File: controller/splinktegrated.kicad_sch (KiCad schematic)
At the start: 41 parts, among them J1 USB_C_Receptacle_USB2.0, J11 Conn_01x07_Socket, J2 Conn_01x04_Socket, J5 Conn_01x02, J7 Cirque, SW2 NA_SW_SPST, U1 RP2040, U3 XC6210B332MR-G, U4 USBLC6-2P6, U5 W25Q128JVS, Y1 Crystal_GND24

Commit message: work
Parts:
- J2: footprint Connector_PinSocket_2.54mm:PinSocket_1x04_P2.54mm_Vertical -> Library:PinSocket_1x04_P2.54mm_Vertical
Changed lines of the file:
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@@
 			)
 		)
-		(property "Footprint" "Connector_PinSocket_2.54mm:PinSocket_1x04_P2.54mm_Vertical"
+		(property "Footprint" "Library:PinSocket_1x04_P2.54mm_Vertical"
 			(at 396.24 38.1 0)
 			(effects

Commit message: Update splinktegrated.kicad_sch
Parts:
- removed SW2: NA_SW_SPST, Library:PushSwitch, symbol Switch:SW_SPST
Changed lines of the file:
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@@
 		)
 	)
-	(label "~{RESET}"
-		(at 44.45 205.105 180)
-		(fields_autoplaced yes)
-		(effects
-			(font
-				(size 1.27 1.27)
-			)
-			(justify right bottom)
-		)
-	)
 	(label "QSPI_~{CS}"
 		(at 111.76 59.69 0)
@@
 	)
 	(symbol
-		(lib_id "Switch:SW_SPST")
-		(at 49.53 205.105 0)
-		(unit 1)
-		(exclude_from_sim no)
-		(in_bom no)
-		(on_board yes)
-		(dnp no)
-		(property "Reference" "SW2"
-			(at 49.53 198.755 0)
-			(effects
-				(font
-					(size 1.27 1.27)
-				)
-			)
-		)
-		(property "Value" "NA_SW_SPST"
-			(at 49.53 201.295 0)
-			(effects
-				(font
-					(size 1.27 1.27)
-				)
-			)
-		)
-		(property "Footprint" "Library:PushSwitch"
-			(at 49.53 205.105 0)
-			(effects
-				(font
-					(size 1.27 1.27)
-				)
-				(hide yes)
-			)
-		)
-		(property "Datasheet" "~"
-			(at 49.53 205.105 0)
-			(effects
-				(font
-					(size 1.27 1.27)
-				)
-				(hide yes)
-			)
-		)
-		(property "Description" ""
-			(at 49.53 205.105 0)
-			(effects
-				(font
-					(size 1.27 1.27)
-				)
-				(hide yes)
-			)
-		)
-		(pin "1"
-		)
-		(pin "2"
-		)
-		(instances
-			(project "splinktegrated"
-				(path "/7353e96a-343a-4876-b497-b1d205a14d97"
-					(reference "SW2")
-					(unit 1)
-				)
-			)
-		)
-	)
-	(symbol
 		(lib_id "power:+1V1")
 		(at 91.44 173.99 0)
@@
 					(unit 1)
 				)
-			)
-		)
-	)
-	(symbol
-		(lib_id "power:GND")
-		(at 54.61 205.105 90)
-		(unit 1)
-		(exclude_from_sim no)
-		(in_bom yes)
-		(on_board yes)
-		(dnp no)
-		(property "Reference" "#PWR05"
-			(at 60.96 205.105 0)
-			(effects
-				(font
-					(size 1.27 1.27)
-				)
-				(hide yes)
-			)
-		)
-		(property "Value" "GND"
-			(at 61.5949 205.261 90)
-			(effects
-				(font
-					(size 1.27 1.27)
-				)
-				(justify left)
-			)
-		)
-		(property "Footprint" ""
-			(at 54.61 205.105 0)
-			(effects
-				(font
-					(size 1.27 1.27)
-				)
-				(hide yes)
-			)
-		)
-		(property "Datasheet" ""
-			(at 54.61 205.105 0)
-			(effects
-				(font
-					(size 1.27 1.27)
-				)
-				(hide yes)
-			)
-		)
-		(property "Description" ""
-			(at 54.61 205.105 0)
-			(effects
-				(font
-					(size 1.27 1.27)
-				)
-				(hide yes)
-			)
-		)
-		(pin "1"
-		)
-		(instances
-			(project "splinktegrated"
-				(path "/7353e96a-343a-4876-b497-b1d205a14d97"
-					(reference "#PWR05")
-					(unit 1)
-				)

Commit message: work
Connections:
- net VBUS renamed Vbus_daughter
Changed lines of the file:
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@@
 	)
 	(junction
-		(at 29.845 29.845)
-		(diameter 0)
-		(color 0 0 0 0)
-	)
-	(junction
 		(at 143.51 38.1)
 		(diameter 0)
@@
 	(wire
 		(pts
-			(xy 27.305 29.845) (xy 29.845 29.845)
+			(xy 27.305 29.845) (xy 32.385 29.845)
 		)
 		(stroke
@@
 		)
 	)
-	(wire
-		(pts
-			(xy 29.845 26.035) (xy 29.845 29.845)
-		)
-		(stroke
-			(width 0)
-			(type default)
-		)
-	)
 	(polyline
 		(pts
@@
 	(wire
 		(pts
-			(xy 29.845 29.845) (xy 32.385 29.845)
-		)
-		(stroke
-			(width 0)
-			(type default)
-		)
-	)
-	(wire
-		(pts
 			(xy 101.6 173.99) (xy 101.6 175.26)
 		)
@@
 					(unit 1)
 				)
-			)
-		)
-	)
-	(symbol
-		(lib_id "power:VBUS")
-		(at 29.845 26.035 0)
-		(unit 1)
-		(exclude_from_sim no)
-		(in_bom yes)
-		(on_board yes)
-		(dnp no)
-		(property "Reference" "#PWR0104"
-			(at 29.845 29.845 0)
-			(effects
-				(font
-					(size 1.27 1.27)
-				)
-				(hide yes)
-			)
-		)
-		(property "Value" "VBUS"
-			(at 29.845 22.225 0)
-			(effects
-				(font
-					(size 1.27 1.27)
-				)
-			)
-		)
-		(property "Footprint" ""
-			(at 29.845 26.035 0)
-			(effects
-				(font
-					(size 1.27 1.27)
-				)
-				(hide yes)
-			)
-		)
-		(property "Datasheet" ""
-			(at 29.845 26.035 0)
-			(effects
-				(font
-					(size 1.27 1.27)
-				)
-				(hide yes)
-			)
-		)
-		(property "Description" ""
-			(at 29.845 26.035 0)
-			(effects
-				(font
-					(size 1.27 1.27)
-				)
-				(hide yes)
-			)
-		)
-		(pin "1"
-		)
-		(instances
-			(project "splinktegrated"
-				(path "/7353e96a-343a-4876-b497-b1d205a14d97"
-					(reference "#PWR0104")
-					(unit 1)
-				)

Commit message: details
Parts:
- removed H1, H2: NA_M4, drawings:MountingHole_3mm_Pad_Via, symbol Mechanical:MountingHole_Pad
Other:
- note removed: "Plate screws"

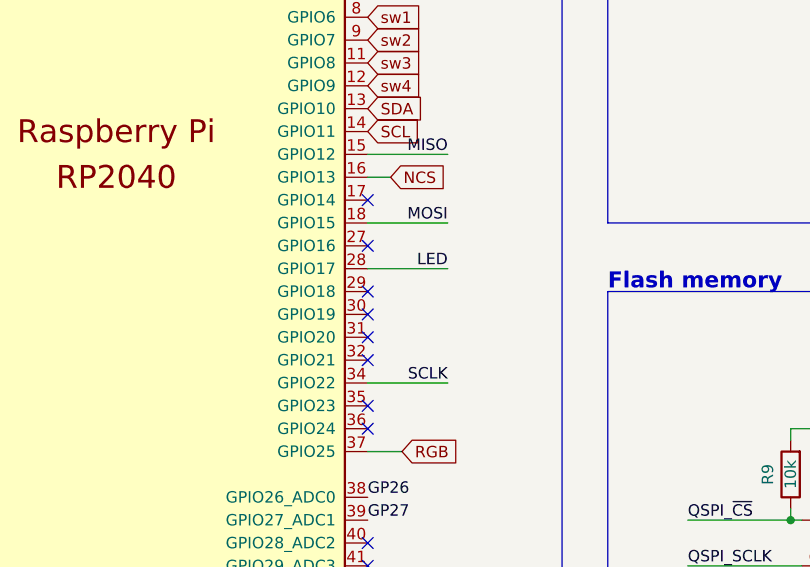
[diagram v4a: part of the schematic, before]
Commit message: change SCK pin
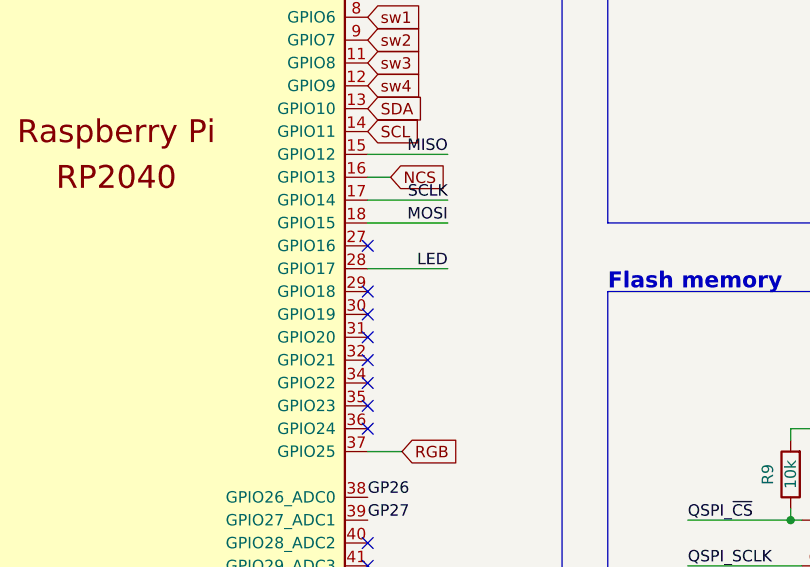
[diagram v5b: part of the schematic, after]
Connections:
- net SCLK: now also U1.17 (GPIO14); no longer U1.34 (GPIO22)
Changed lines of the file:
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@@
 	)
 	(no_connect
-		(at 182.88 93.98)
+		(at 182.88 114.3)
 	)
 	(no_connect
@@
 	(wire
 		(pts
-			(xy 182.88 114.3) (xy 191.77 114.3)
+			(xy 182.88 93.98) (xy 191.77 93.98)
 		)
 		(stroke
@@
 	)
 	(label "SCLK"
-		(at 191.77 114.3 180)
+		(at 191.77 93.98 180)
 		(fields_autoplaced yes)
 		(effects

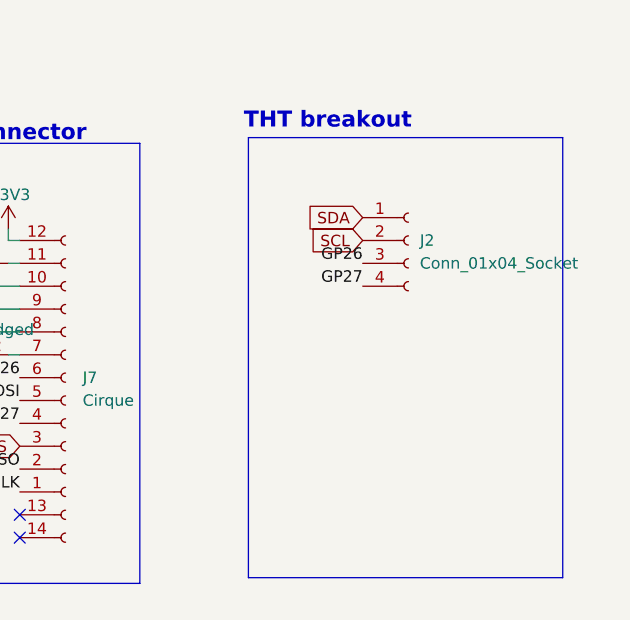
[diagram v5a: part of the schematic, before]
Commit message: add trackpad breakouts
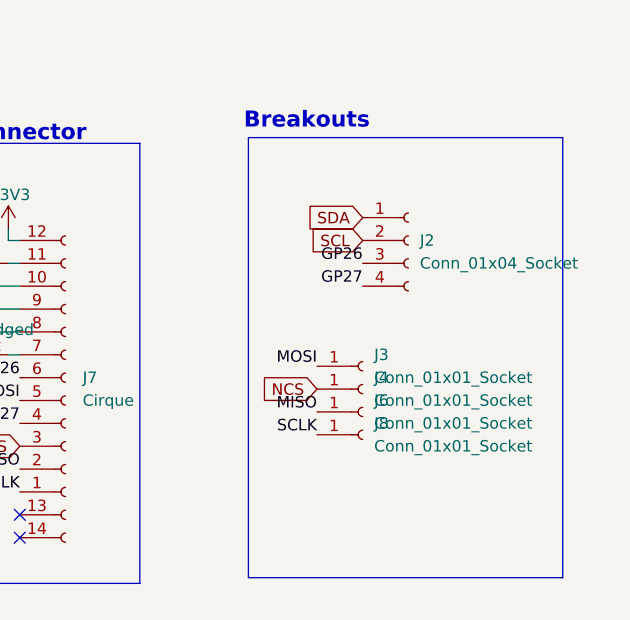
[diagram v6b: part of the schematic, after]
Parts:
- added J3, J4, J6, J8: Conn_01x01_Socket, drawings:PinHeader_1x01_P1.27mm_SMD, symbol Connector:Conn_01x01_Socket
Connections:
- net MISO: now also J6.1 (Pin_1)
- net MOSI: now also J3.1 (Pin_1)
- net NCS: now also J4.1 (Pin_1)
- net SCLK: now also J8.1 (Pin_1)
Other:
- note added: "Breakouts"
- note removed: "THT breakout"
